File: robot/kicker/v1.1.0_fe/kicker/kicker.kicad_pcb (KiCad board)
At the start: 4 copper layers, 76 x 90 mm, 139 parts, among them J1 XT30PW-M, J2 1054052108, J3 2157601002, J4 2157601002, J5 Conn_ARM_JTAG_SWD_10, J6 Conn_01x03_Female, J7 Conn_01x03, J8 Conn_01x03, Q1 BSC0402NSATMA1, Q2 IXGA48N60A3, Q3 IXGA48N60A3, Q4 BSS138K, U1 LM1117-5.0, U2 LM1117-3.3, U3 ADUM7441, U4 LT3751-QFN, U5 IX4427, U6 STM32F030K6Tx, U7 SK9822, U8 SK9822

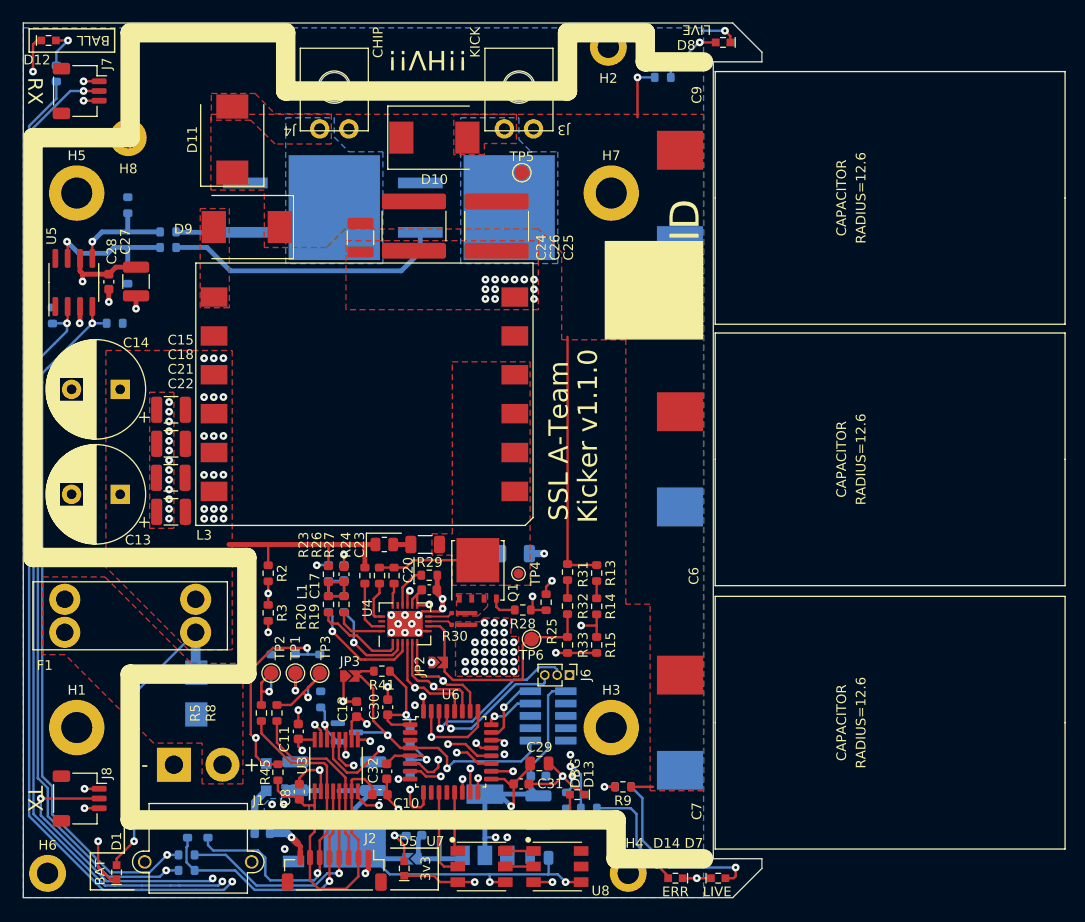
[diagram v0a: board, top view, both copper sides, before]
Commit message: kicker fixes, 1.1.0 tssop variant
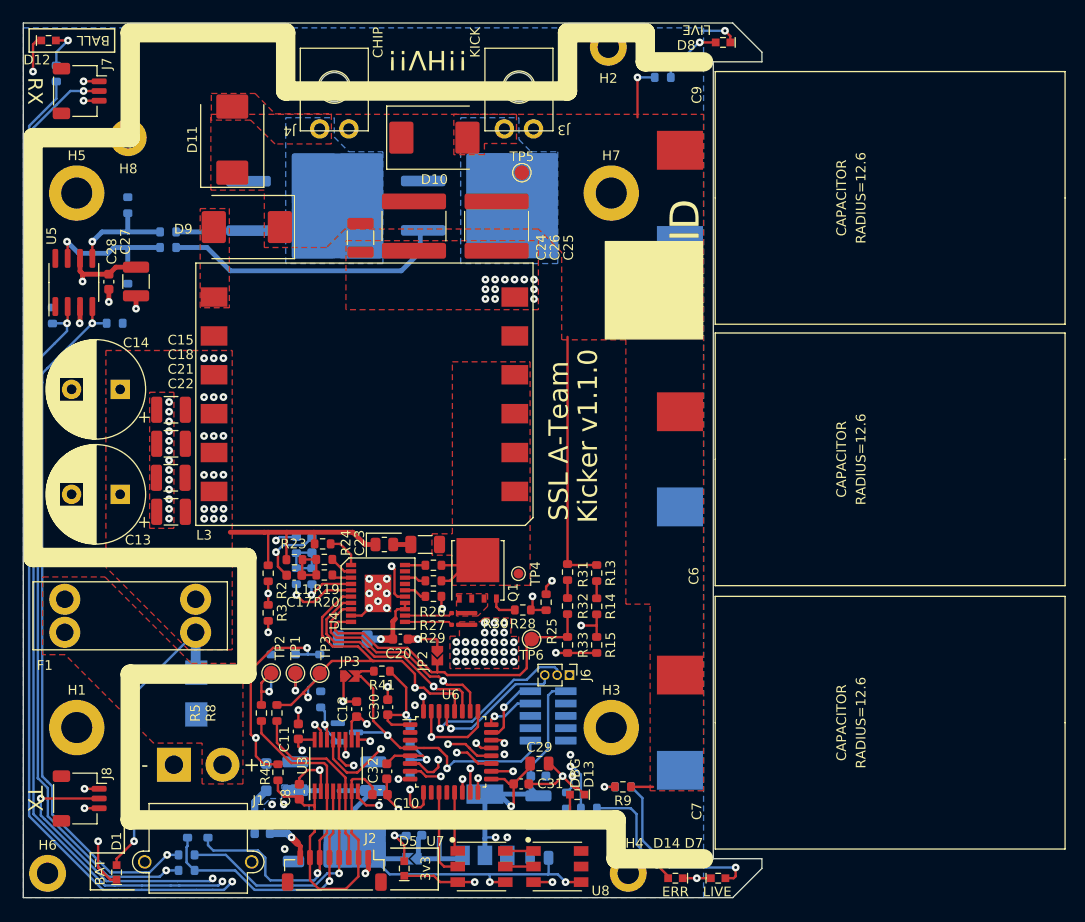
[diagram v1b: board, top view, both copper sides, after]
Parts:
- U4: value LT3751-QFN -> LT3751; footprint AT-IC:LT3751-QFN20_EP_4x5mm_P0.5mm -> AT-IC:LT3751-FE
- moved C16 18.9 mm to (210.9, 168.4)
- moved C20 5.88 mm to (215.8, 168.4)
- moved R26 5.65 mm to (219.2, 160.8), turned to 0 degrees
- moved R23 5.44 mm to (207.8, 158.6), turned to 180 degrees
- moved C17 5.13 mm to (204.9, 161.8), turned to 180 degrees
- moved R19 5.05 mm to (208.0, 160.2), turned to 0 degrees
- moved R21 4.38 mm to (206.7, 161.9)
- moved R22 4.38 mm to (205.1, 161.9)
- moved C19 4.38 mm to (206.7, 158.7)
- moved L2 4.38 mm to (205.1, 158.7)
- moved U4 4.18 mm to (213.5, 163.7), turned to -90 degrees
- moved R27 4.09 mm to (219.2, 162.4), turned to 0 degrees
- moved L1 3.81 mm to (204.9, 160.2), turned to 0 degrees
- moved R20 3.05 mm to (208.0, 161.8), turned to 0 degrees
- moved R29 2.22 mm to (219.2, 164.0)
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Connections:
- U4 pad 1: /flyback_charger/OVLO1 -> /flyback_charger/RV_{trans}
- U4 pad 10: /flyback_charger/CSP -> /flyback_charger/FB
- U4 pad 11: +12V -> /flyback_charger/CSN
- U4 pad 12: +12V -> /flyback_charger/CSP
- U4 pad 13: /flyback_charger/HVGATE -> +12V
- U4 pad 14: /flyback_charger/RBG -> +12V
- U4 pad 15: unconnected-(U4-NC1-Pad15) -> /flyback_charger/HVGATE
- U4 pad 16: /flyback_charger/RV_{out} -> /flyback_charger/RBG
- U4 pad 17: /flyback_charger/RDCM -> unconnected-(U4-NC1-Pad17)
- U4 pad 18: unconnected-(U4-NC2-Pad18) -> /flyback_charger/RV_{out}
- U4 pad 19: /flyback_charger/RV_{trans} -> unconnected-(U4-NC2-Pad19)
- U4 pad 2: /flyback_charger/UVLO2 -> /flyback_charger/UVLO1
- U4 pad 20: /flyback_charger/UVLO1 -> /flyback_charger/RDCM
- U4 pad 3: /flyback_charger/OVLO2 -> /flyback_charger/OVLO1
- U4 pad 4: /STATUS_{~{FAULT}} -> /flyback_charger/UVLO2
- U4 pad 5: /STATUS_{~{DONE}} -> /flyback_charger/OVLO2
- U4 pad 6: /CMD_{CHG} -> /STATUS_{~{FAULT}}
- U4 pad 7: GND -> /STATUS_{~{DONE}}
- U4 pad 8: /flyback_charger/FB -> /CMD_{CHG}
- U4 pad 9: /flyback_charger/CSN -> GND
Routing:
- net +12V: track 208.2 -> 187.4 mm, vias 6 -> 5
- net /STATUS_{~{FAULT}}: track 32.4 -> 51.9 mm
- net /STATUS_{~{DONE}}: track 30.1 -> 42.0 mm
- net /CMD_{CHG}: track 36.9 -> 48.1 mm
- net /flyback_charger/FB: track 25.3 -> 34.6 mm
- net /flyback_charger/OVLO1: track 9.50 -> 2.04 mm
- net /flyback_charger/HVGATE: track 19.4 -> 26.4 mm
- net /flyback_charger/OVLO2: track 11.8 -> 7.52 mm
- net /flyback_charger/UVLO2: track 9.60 -> 5.66 mm
- net GND: track 85.7 -> 89.4 mm, vias 93 -> 91
- net /flyback_charger/UVLO1: track 5.35 -> 2.43 mm
- net /flyback_charger/CSN: track 2.54 -> 4.92 mm
- net /flyback_charger/CSP: track 2.54 -> 4.90 mm
- net /flyback_charger/RDCM: track 4.40 -> 2.11 mm
- net /flyback_charger/RV_{trans}: track 5.70 -> 3.62 mm
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
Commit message: NEED KCv7.1 DRC check - silk and redundant routing fixed, v7.0
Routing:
- net /STATUS_{~{FAULT}}: track 51.9 -> 37.1 mm, vias 2 -> 1
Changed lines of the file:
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@@
     (property "ki_keywords" "R res resistor")
     (attr smd exclude_from_pos_files)
-    (fp_text reference "R8" (at 0 -6.8 90) (layer "F.SilkS")
+    (fp_text reference "R8" (at 0 -3 90) (layer "F.SilkS")
         (effects (font (size 1 1) (thickness 0.15)))
     )
@@
     (property "ki_keywords" "R res resistor")
     (attr smd exclude_from_pos_files)
-    (fp_text reference "R5" (at 0 -6.8 90) (layer "F.SilkS")
+    (fp_text reference "R5" (at 0 -3 90) (layer "F.SilkS")
         (effects (font (size 1 1) (thickness 0.15)))
     )
@@
     (effects (font (size 1 1) (thickness 0.15)))
   )
-  (gr_text "DBG" (at 233.8 182.2 90) (layer "F.SilkS")
+  (gr_text "DBG" (at 231 185) (layer "F.SilkS")
     (effects (font (size 1 1) (thickness 0.15)))
   )
@@
   (segment (start 178.94856 141.05144) (end 178.94856 142) (width 0.25) (layer "B.Cu") (net 35))
   (segment (start 179.974031 183.540234) (end 179.974031 185.7) (width 0.25) (layer "B.Cu") (net 35))
-  (segment (start 220.463323 173.99904) (end 221.19904 173.99904) (width 0.25) (layer "F.Cu") (net 36))
-  (segment (start 213.1 170.65) (end 208.75 170.65) (width 0.25) (layer "F.Cu") (net 36))
   (segment (start 205.812307 173.912307) (end 206.3 174.4) (width 0.25) (layer "F.Cu") (net 36))
-  (segment (start 221.19904 173.99904) (end 221.4 174.2) (width 0.25) (layer "F.Cu") (net 36))
+  (segment (start 221.38 175.825) (end 221.4 175.805) (width 0.25) (layer "F.Cu") (net 36))
+  (segment (start 221.19904 173.99904) (end 218.924407 173.99904) (width 0.25) (layer "F.Cu") (net 36))
   (segment (start 209.875 164.025) (end 210.725 164.025) (width 0.25) (layer "F.Cu") (net 36))
   (segment (start 203.1 175.175) (end 204.549614 175.175) (width 0.25) (layer "F.Cu") (net 36))
-  (segment (start 213.1 170.65) (end 212.940812 170.65) (width 0.25) (layer "F.Cu") (net 36))
-  (segment (start 220.463323 173.99904) (end 218.823654 173.99904) (width 0.25) (layer "F.Cu") (net 36))
-  (segment (start 215.964276 170.65) (end 213.1 170.65) (width 0.25) (layer "F.Cu") (net 36))
-  (segment (start 218.224614 173.4) (end 217.3 173.4) (width 0.25) (layer "F.Cu") (net 36))
-  (segment (start 211.440812 169.15) (end 208.840812 169.15) (width 0.25) (layer "F.Cu") (net 36))
+  (segment (start 207.5 169.5) (end 208.345406 168.654594) (width 0.25) (layer "F.Cu") (net 36))
   (segment (start 204.549614 175.175) (end 205.812307 173.912307) (width 0.25) (layer "F.Cu") (net 36))
-  (segment (start 217.3 173.4) (end 217.3 171.985724) (width 0.25) (layer "F.Cu") (net 36))
-  (segment (start 208.840812 169.15) (end 207.75 168.059188) (width 0.25) (layer "F.Cu") (net 36))
-  (segment (start 218.823654 173.99904) (end 218.562307 173.737693) (width 0.25) (layer "F.Cu") (net 36))
+  (segment (start 208.345406 168.654594) (end 207.75 168.059188) (width 0.25) (layer "F.Cu") (net 36))
+  (segment (start 208.840812 169.15) (end 208.345406 168.654594) (width 0.25) (layer "F.Cu") (net 36))
+  (segment (start 221.4 175.805) (end 221.4 174.2) (width 0.25) (layer "F.Cu") (net 36))
   (segment (start 205.812307 173.912307) (end 207.5 172.224614) (width 0.25) (layer "F.Cu") (net 36))
-  (segment (start 217.3 171.985724) (end 215.964276 170.65) (width 0.25) (layer "F.Cu") (net 36))
+  (segment (start 207.5 171.9) (end 207.5 169.5) (width 0.25) (layer "F.Cu") (net 36))
+  (segment (start 218.924407 173.99904) (end 215.575367 170.65) (width 0.25) (layer "F.Cu") (net 36))
   (segment (start 207.5 172.224614) (end 207.5 171.9) (width 0.25) (layer "F.Cu") (net 36))
+  (segment (start 215.575367 170.65) (end 212.940812 170.65) (width 0.25) (layer "F.Cu") (net 36))
+  (segment (start 211.440812 169.15) (end 208.840812 169.15) (width 0.25) (layer "F.Cu") (net 36))
   (segment (start 207.75 168.059188) (end 207.75 166.15) (width 0.25) (layer "F.Cu") (net 36))
-  (segment (start 212.940812 170.65) (end 211.440812 169.15) (width 0.25) (layer "F.Cu") (net 36))
-  (segment (start 221.4 175.805) (end 221.38 175.825) (width 0.25) (layer "F.Cu") (net 36))
   (segment (start 207.75 166.15) (end 209.875 164.025) (width 0.25) (layer "F.Cu") (net 36))
-  (segment (start 208.75 170.65) (end 207.5 171.9) (width 0.25) (layer "F.Cu") (net 36))
-  (segment (start 221.4 174.2) (end 221.4 175.805) (width 0.25) (layer "F.Cu") (net 36))
-  (segment (start 218.562307 173.737693) (end 218.224614 173.4) (width 0.25) (layer "F.Cu") (net 36))
+  (segment (start 212.940812 170.65) (end 211.440812 169.15) (width 0.25) (layer "F.Cu") (net 36))
+  (segment (start 221.4 174.2) (end 221.19904 173.99904) (width 0.25) (layer "F.Cu") (net 36))
   (via (at 206.3 174.4) (size 0.8) (drill 0.3) (layers "F.Cu" "B.Cu") (net 36))
-  (via (at 217.3 173.4) (size 0.8) (drill 0.3) (layers "F.Cu" "B.Cu") (net 36))
-  (segment (start 206.3 174.4) (end 206.624511 174.075489) (width 0.25) (layer "In1.Cu") (net 36))
-  (segment (start 216.624511 174.075489) (end 217.3 173.4) (width 0.25) (layer "In1.Cu") (net 36))
-  (segment (start 206.624511 174.075489) (end 216.624511 174.075489) (width 0.25) (layer "In1.Cu") (net 36))
   (segment (start 207.5 171.625) (end 207.5 172.2) (width 0.25) (layer "B.Cu") (net 36))
   (segment (start 207.5 172.2) (end 206.3 173.4) (width 0.25) (layer "B.Cu") (net 36))
